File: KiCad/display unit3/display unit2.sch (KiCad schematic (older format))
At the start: 44 parts, among them J1 Conn_01x03_Female, J2 Conn_01x03_Female, Q1 BC547, Q2 BC547, Q3 BC547, U1 LM358, U2 LM358

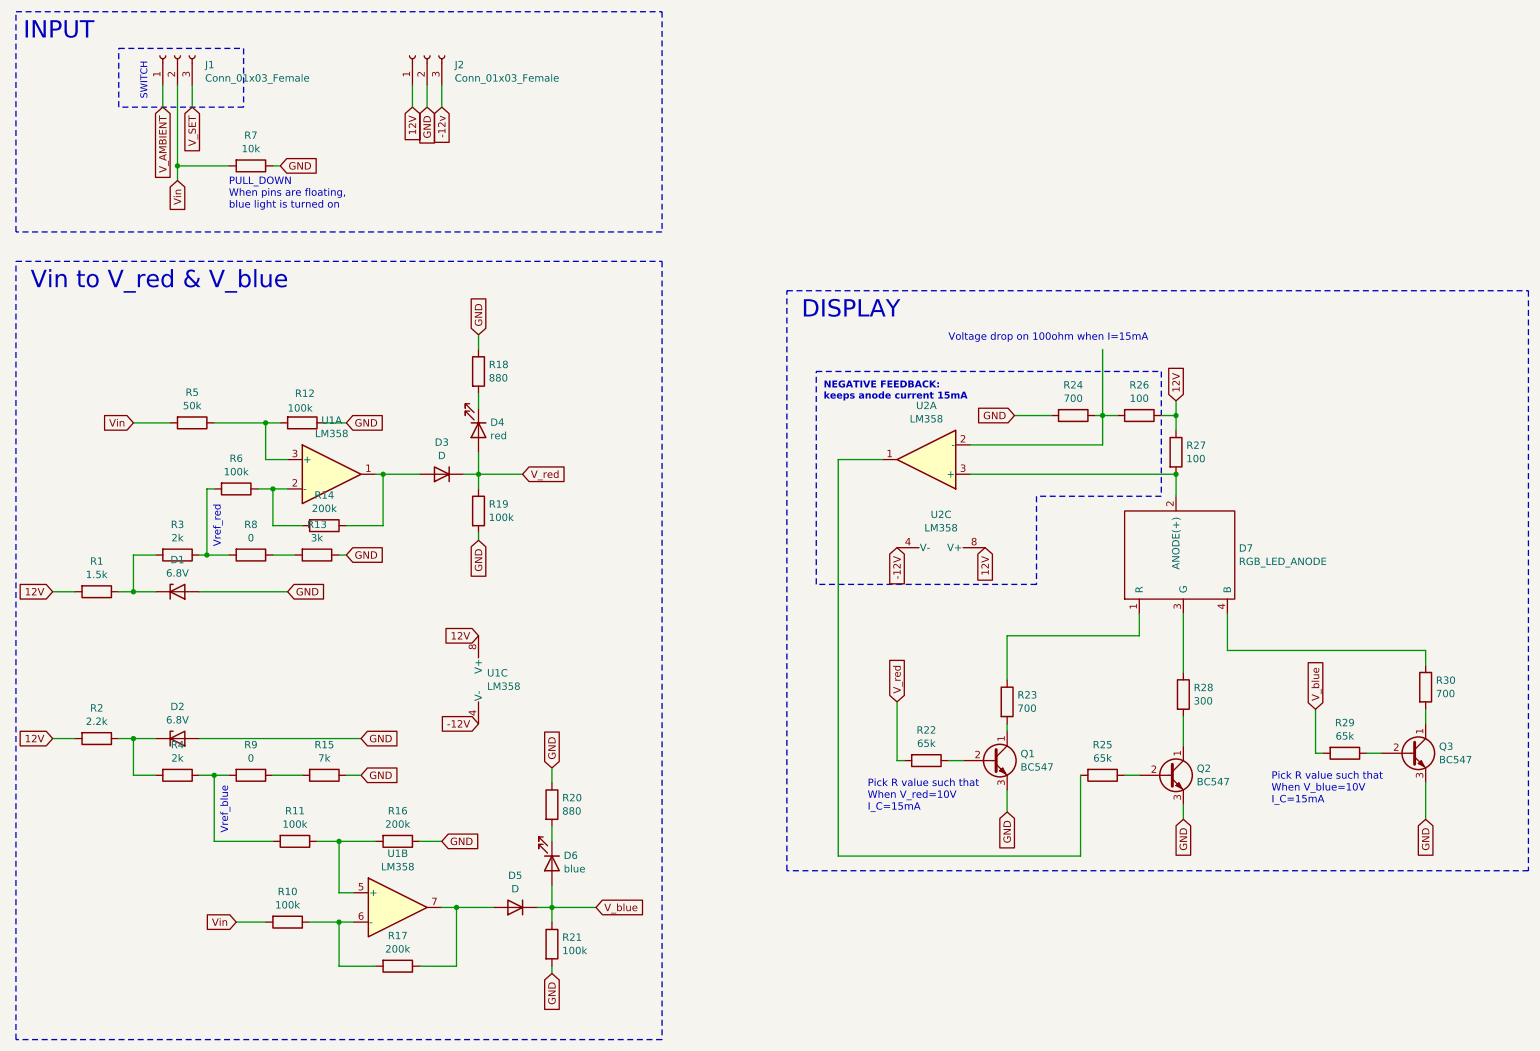
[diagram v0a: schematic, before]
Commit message: display unit 3 PCB is finished
.
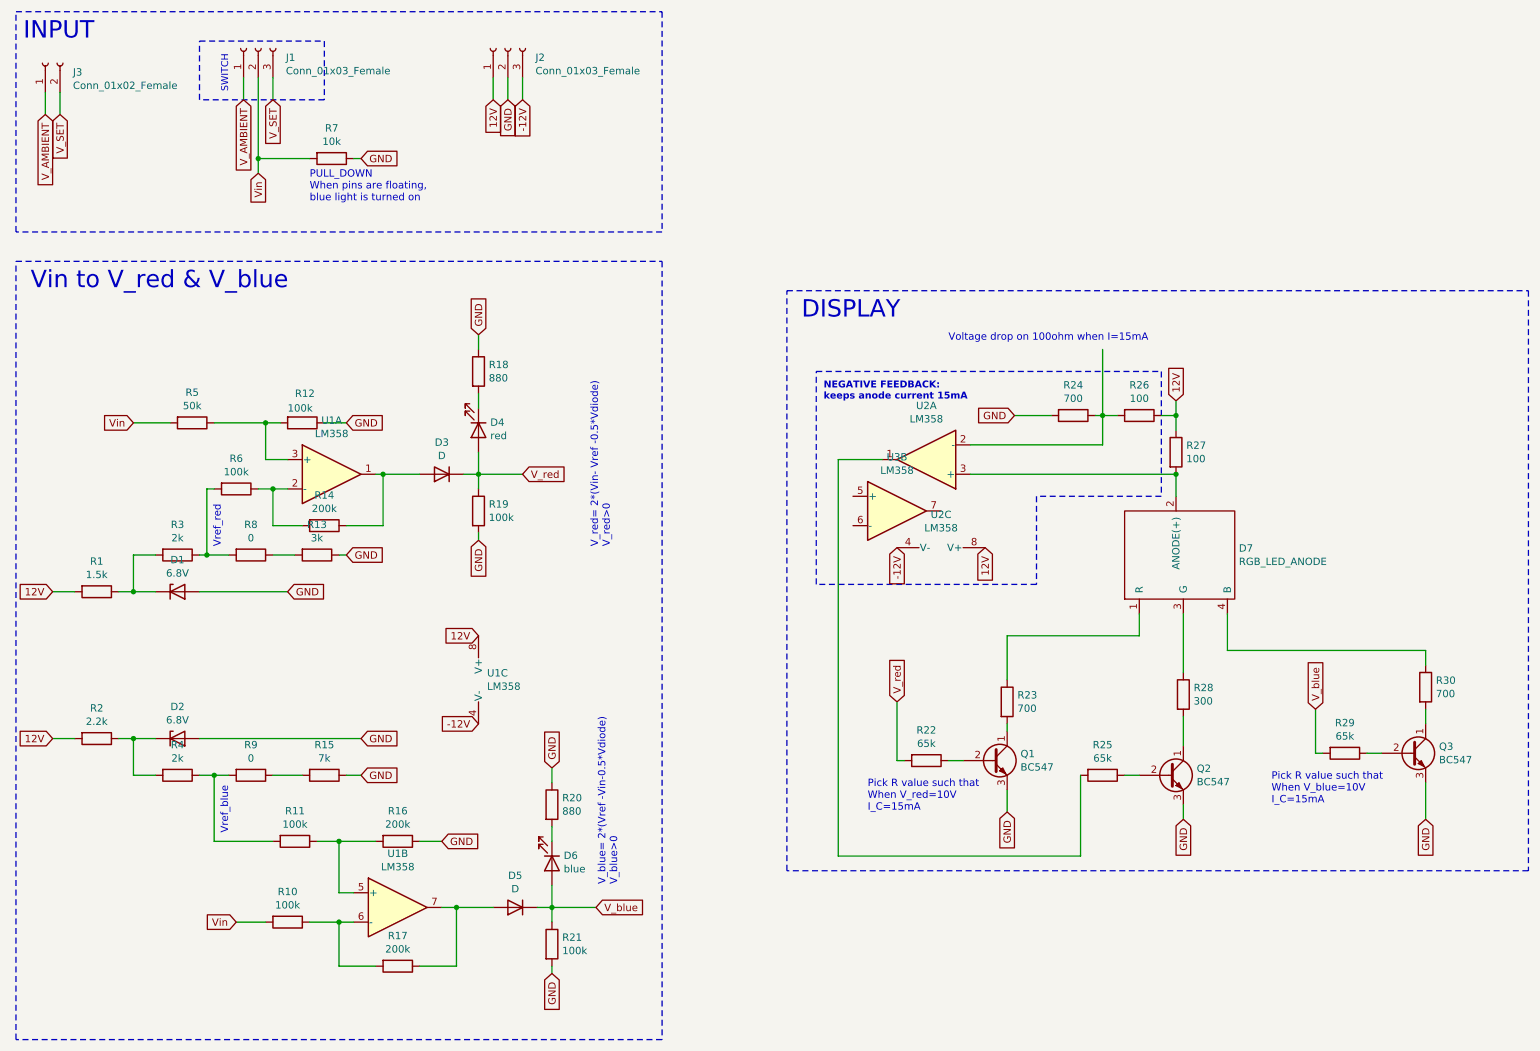
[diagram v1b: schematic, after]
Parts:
- added J3: Conn_01x02_Female, TerminalBlock:TerminalBlock_Altech_AK300-2_P5.00mm, symbol Connector:Conn_01x02_Female
- added U3: LM358, symbol Amplifier_Operational:LM358
- D1, D2, D3, D5: footprint (none) -> Diode_THT:D_A-405_P12.70mm_Horizontal
- D4, D6: footprint (none) -> LED_THT:LED_D3.0mm_FlatTop
- D7: footprint (none) -> Connector_PinHeader_2.54mm:PinHeader_1x04_P2.54mm_Vertical
- J1: footprint (none) -> Connector_PinHeader_2.54mm:PinHeader_1x03_P2.54mm_Vertical
- J2: footprint (none) -> TerminalBlock:TerminalBlock_Altech_AK300-3_P5.00mm
- Q1, Q2, Q3: footprint Package_TO_SOT_THT:TO-92_Inline -> Package_TO_SOT_THT:TO-92L_Inline_Wide
- R1, R10, R11, R12, R13, R14, R15, R16, R17, R18, R19, R2, R20, R21, R22, R23, R24, R25, R26, R27, R28, R29, R3, R30, R4, R5, R6, R7, R8, R9: footprint (none) -> Resistor_THT:R_Axial_DIN0309_L9.0mm_D3.2mm_P12.70mm_Horizontal
- U1, U2: footprint (none) -> Package_DIP:DIP-8_W7.62mm
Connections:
- net -12v is gone; now on net -12V: J2.3 (Pin_3)
- net V_AMBIENT: now also J3.1 (Pin_1)
- net V_SET: now also J3.2 (Pin_2)
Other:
- note added: "V_blue= 2*(Vref -Vin-0.5*Vdiode)\nV_blue>0\n"
- note added: "V_red= 2*(Vin- Vref -0.5*Vdiode)\nV_red>0\n"
- moved on the sheet: J1, J2, R7
